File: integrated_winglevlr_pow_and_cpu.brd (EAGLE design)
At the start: 53.3 x 11.9 mm, 13 parts

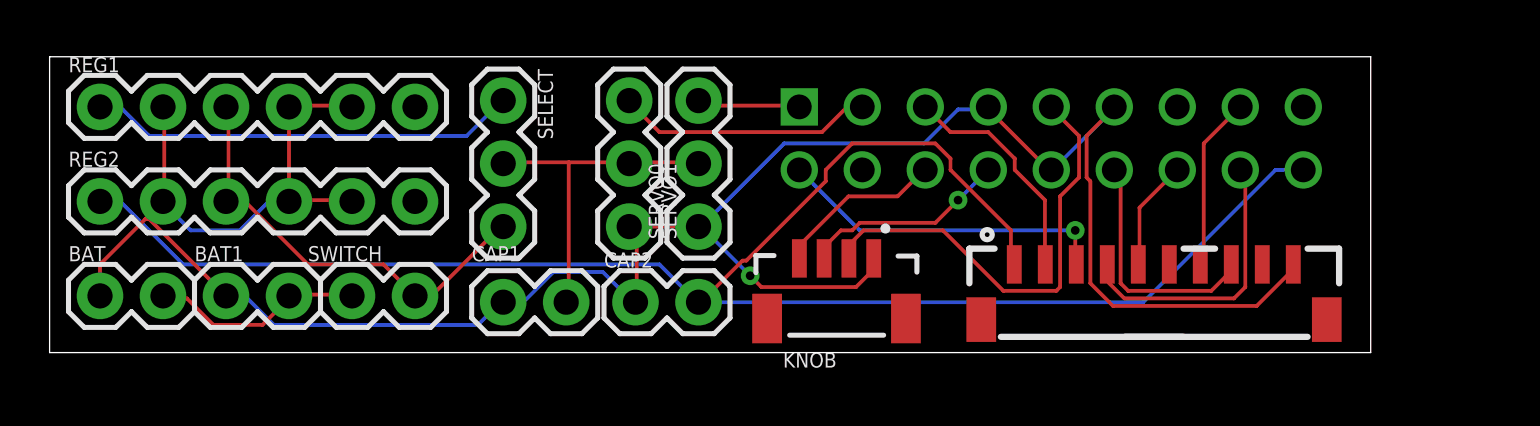
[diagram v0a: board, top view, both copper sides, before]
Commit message: Add I2C connector
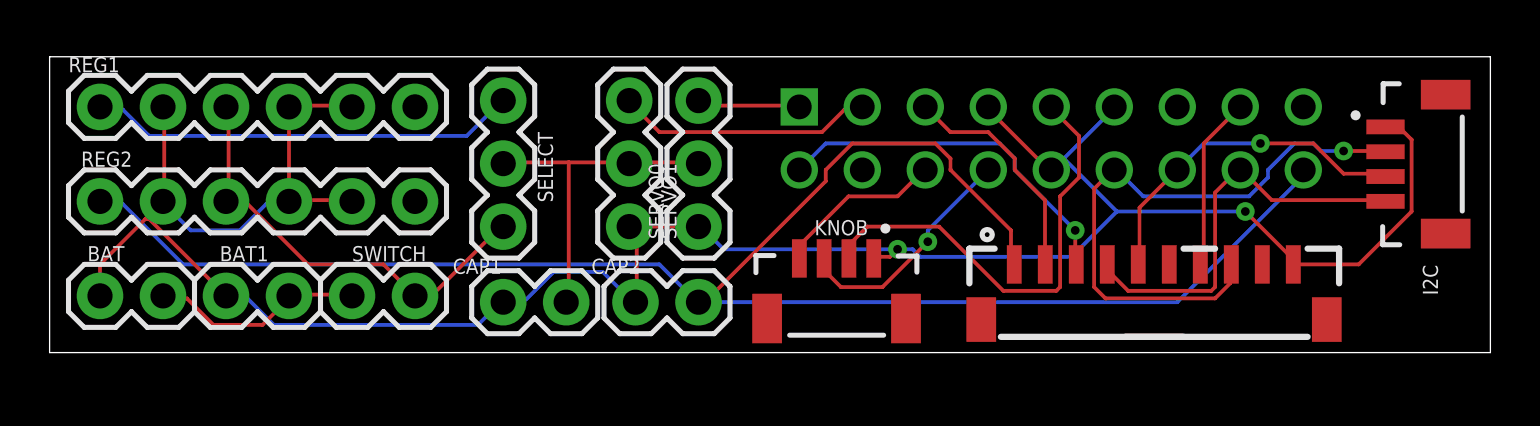
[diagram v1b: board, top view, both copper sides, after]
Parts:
- added I2C: Vertical Qwiic Connector, SparkFun-Connectors:JST04_1MM_VERT
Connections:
- net GND: now also I2C.1
- net SCL1: now also I2C.4
- net SDA1: now also I2C.3
- net VCC_33: now also I2C.2
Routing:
- net VCC_33: track 9.95 -> 24.4 mm, vias 0 -> 1
- net SDA1: track 4.49 -> 13.9 mm, vias 0 -> 1
- net SCL1: track 11.6 -> 16.6 mm
- net GND: track 99.4 -> 100.8 mm, vias 1 -> 2
- net KROT1: track 8.36 -> 9.60 mm
- net GPS_RX: track 13.5 -> 14.7 mm
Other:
- board size 53.3 x 11.9 mm -> 58.1 x 11.9 mm
